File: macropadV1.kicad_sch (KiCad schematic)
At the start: 56 parts, among them SW1 SW_Push, U1 ATmega32U4-A, Y1 16MHz

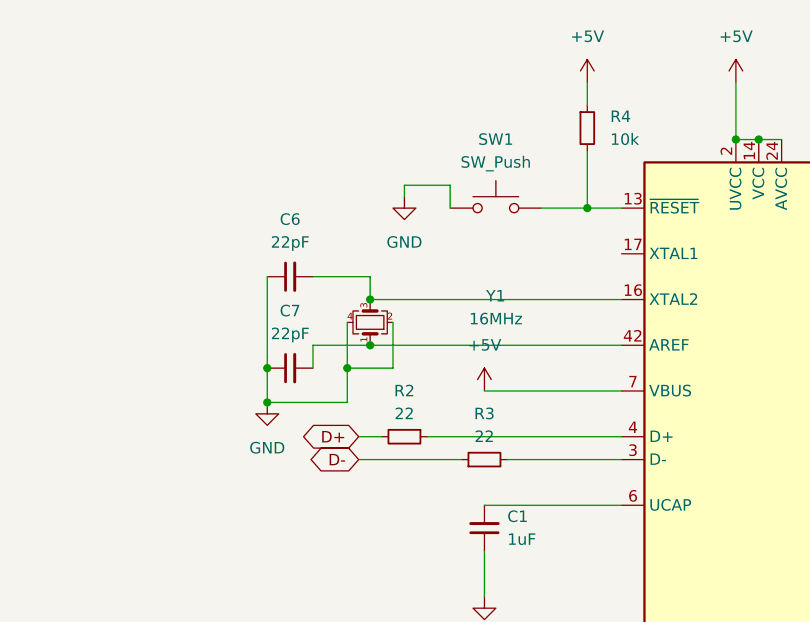
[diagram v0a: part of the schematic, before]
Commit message: Schematic done
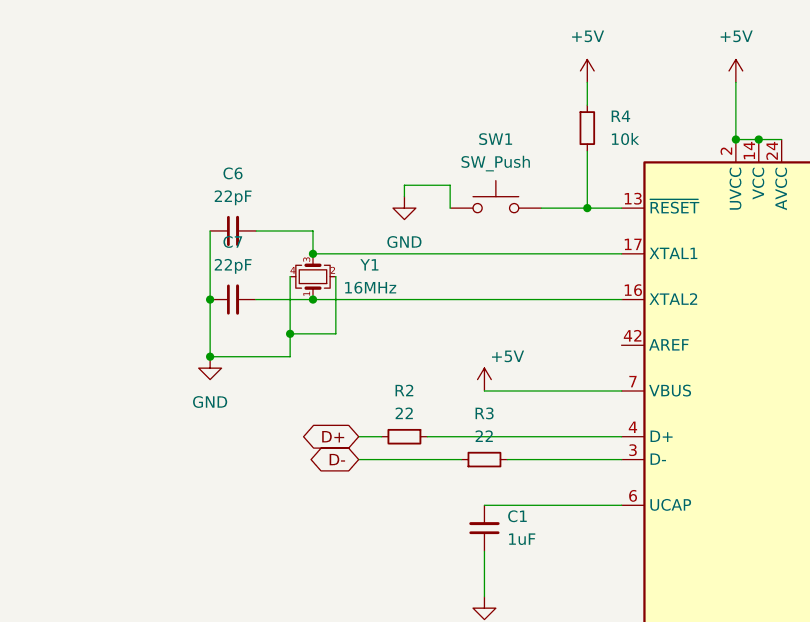
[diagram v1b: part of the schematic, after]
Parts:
- C1, C2, C3, C4, C5, C6, C7: footprint (none) -> Capacitor_SMD:C_0805_2012Metric
- D1, D10, D11, D12, D13, D14, D15, D16, D17, D18, D19, D2, D20, D3, D4, D5, D6, D7, D8, D9: footprint (none) -> Diode_SMD:D_0805_2012Metric
- F1: footprint (none) -> Fuse:Fuse_1206_3216Metric
- MX1, MX10, MX11, MX12, MX13, MX14, MX15, MX16, MX17, MX18, MX19, MX2, MX3, MX4, MX5, MX6, MX7, MX8, MX9: footprint (none) -> MX_Only:MXOnly-1U
- MX20, R1, R2, R3, R4: footprint (none) -> Resistor_SMD:R_0805_2012Metric
- SW1: footprint (none) -> random-keyboard-parts:SKQG-1155865
- USB1: footprint (none) -> random-keyboard-parts:Molex-0548190589
- Y1: footprint (none) -> Crystal:Crystal_SMD_3225-4Pin_3.2x2.5mm
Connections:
- net at C6.2, Y1.3: now also U1.17 (XTAL1); no longer U1.16 (XTAL2)
- net at C7.2, Y1.1: now also U1.16 (XTAL2); no longer U1.42 (AREF)
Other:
- moved on the sheet: C6, C7, Y1

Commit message: Save
just a save in between
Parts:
- MX20: footprint Resistor_SMD:R_0805_2012Metric -> MX_Only:MXOnly-1U
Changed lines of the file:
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@@
       (effects (font (size 0.508 0.508)))
     )
-    (property "Footprint" "Resistor_SMD:R_0805_2012Metric" (at 230.505 144.145 0)
+    (property "Footprint" "MX_Only:MXOnly-1U" (at 230.505 144.145 0)
       (effects (font (size 1.524 1.524)) hide)
     )
